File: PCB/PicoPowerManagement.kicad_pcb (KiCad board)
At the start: 2 copper layers, 101 x 71.5 mm, 21 parts, among them J1 Raspberry Pi 5 GPIO, J10 UART Header, J11 ATX 24P Connection, J12 Pi Power, J13 Barrel_Jack, J2 Raspberry Pi Pico, J3 DisplayPowerSwitch, J4 Pi1PowerSwitch, J5 Pi2PowerSwitch, J6 Pi4PowerSwitch, J7 NAS Fan 1, J8 NAS Fan 2, J9 Pi3PowerSwitch, Q1 2N3904, SW1 Power, U1 LSF0101DRYR, U2 LSF0101DRYR

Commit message: Add initial implementation of PicoPowerManagement project with API and client setup
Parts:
- removed J1: Raspberry Pi 5 GPIO, Connector_PinHeader_2.54mm:PinHeader_2x20_P2.54mm_Vertical
- J12: footprint Connector_PinHeader_2.54mm:PinHeader_2x05_P2.54mm_Vertical -> Connector_PinHeader_2.54mm:PinHeader_2x10_P2.54mm_Vertical
- moved Q1 4.09 mm to (134.0, 76.0)
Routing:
- net +5V: track 159.3 -> 148.0 mm
- net /PSU_ON: track 24.4 -> 28.0 mm
- net /PS_ON#: track 6.46 -> 8.97 mm
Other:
- board size 101 x 71.5 mm -> 78 x 70.5 mm

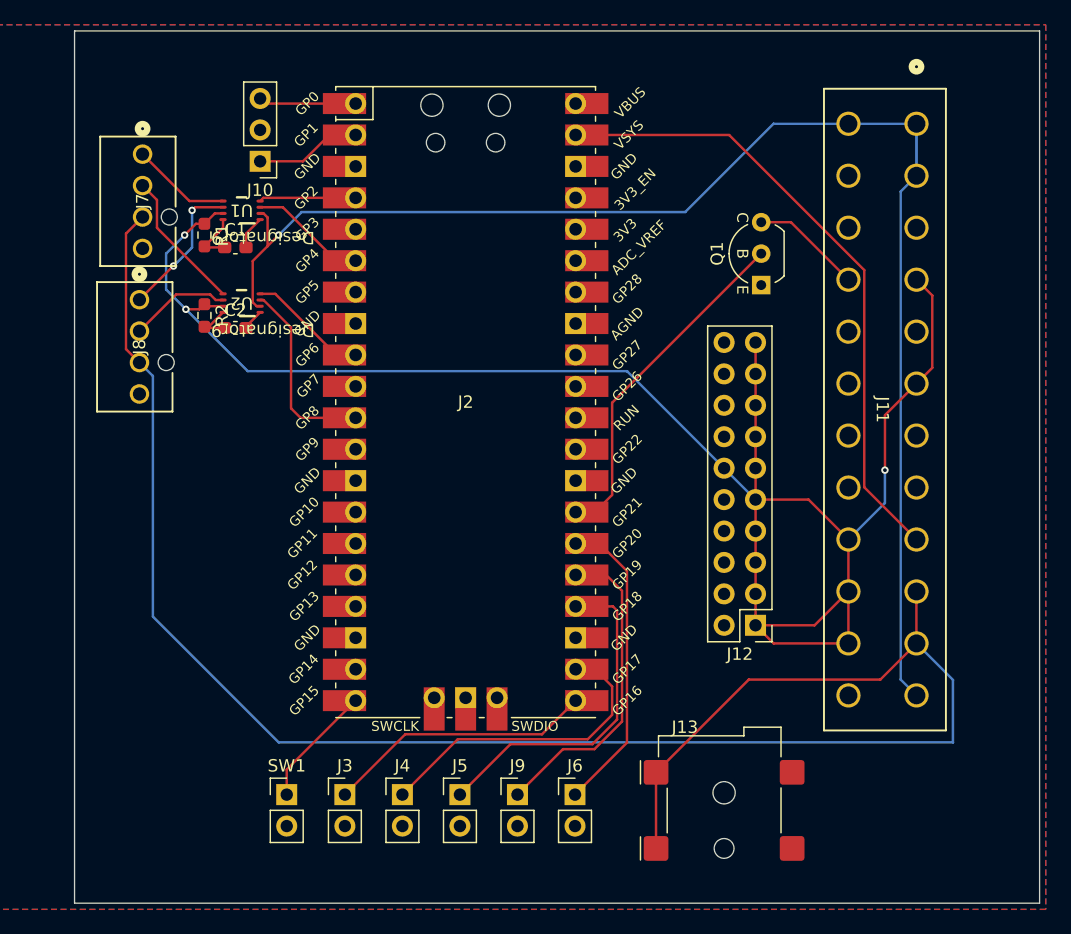
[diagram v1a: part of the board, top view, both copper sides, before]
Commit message: Add UART and pin setup functionality for PicoPowerManagement project
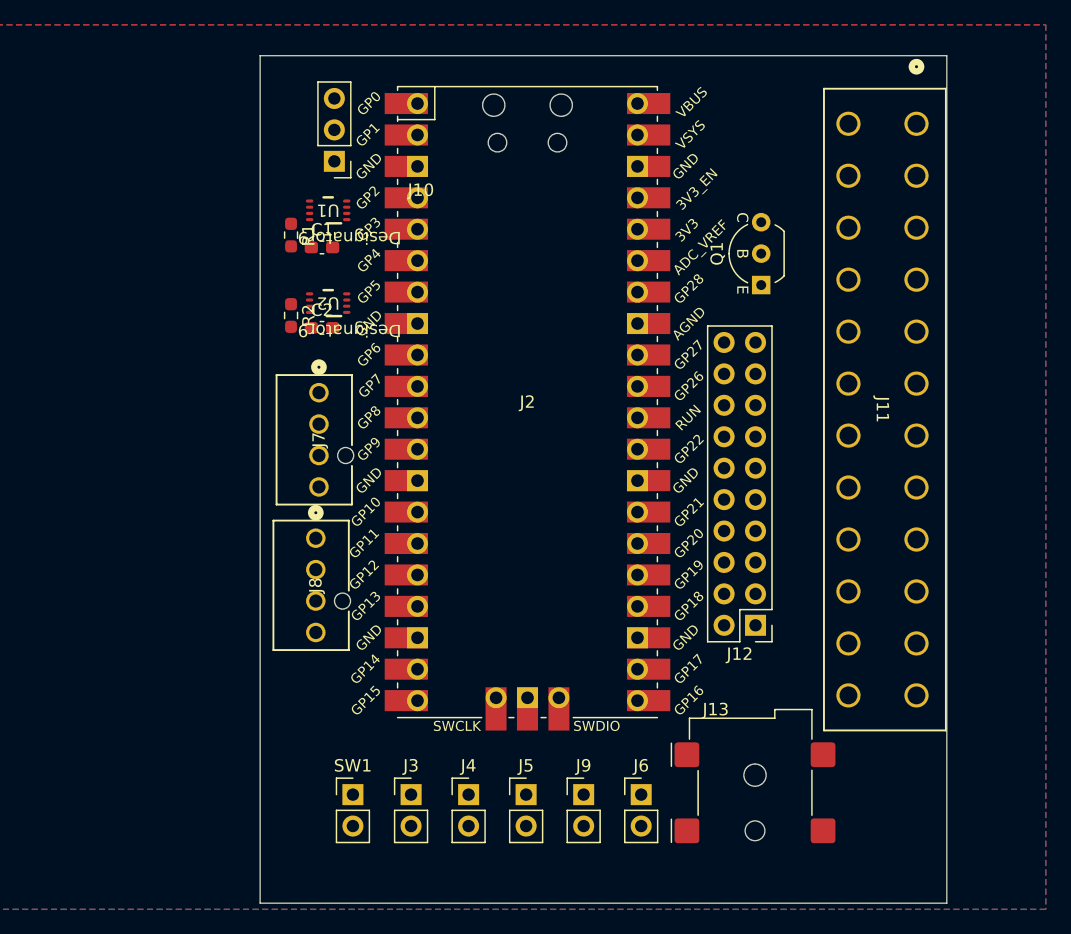
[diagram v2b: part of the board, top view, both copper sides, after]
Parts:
- moved J7 24.0 mm to (98.3, 84.7)
- moved J8 24.0 mm to (98.0, 96.5)
- moved C1 7.00 mm to (98.5, 73.0)
- moved C2 7.00 mm to (98.5, 79.5)
- moved R1 7.00 mm to (96.0, 72.0)
- moved R2 7.00 mm to (96.0, 78.5)
- moved U1 7.00 mm to (99.0, 70.0)
- moved U2 7.00 mm to (99.0, 77.5)
- moved J10 6.00 mm to (99.5, 66.0)
- moved J3 5.35 mm to (105.7, 117.2)
- moved J9 5.35 mm to (119.7, 117.2)
- moved J4 5.35 mm to (110.3, 117.2)
- moved J5 5.35 mm to (115.0, 117.2)
- moved J6 5.35 mm to (124.3, 117.2)
- moved SW1 5.35 mm to (101.0, 117.2)
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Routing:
- net +5V: track 148.0 -> 0.00 mm, vias 3 -> 0
- net +12V: track 147.6 -> 0.00 mm
- net +3.3V: track 112.6 -> 0.00 mm, vias 1 -> 0
- net /+5VDC_Standby: track 51.4 -> 0.00 mm
- net /PSU_ON: track 28.0 -> 0.00 mm
- net /Pi2_On: track 27.5 -> 0.00 mm
- net /Pi3_On: track 25.7 -> 0.00 mm
- net /Pi1_On: track 25.4 -> 0.00 mm
- net /Pi4_On: track 24.9 -> 0.00 mm
- net /Display_On: track 21.8 -> 0.00 mm
- net /3v3RPMSignal2: track 15.5 -> 0.00 mm
- net /5V PWM2: track 11.6 -> 0.00 mm, vias 2 -> 0
- net /RPM Signal1: track 11.4 -> 0.00 mm
- net Net-(J2-GPIO15): track 9.90 -> 0.00 mm
- net /3v3RPMSignal1: track 9.77 -> 0.00 mm
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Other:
- board size 78 x 70.5 mm -> 55.5 x 68.5 mm

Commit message: revamping
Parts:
- removed SW1: Power, Connector_PinHeader_2.54mm:PinHeader_1x02_P2.54mm_Vertical
- added C10: 0.1uF, Capacitor_SMD:C_0603_1608Metric_Pad1.08x0.95mm_HandSolder, F.Cu at (238.3, 32.9)
- added C11: 200pF, Capacitor_SMD:C_0603_1608Metric_Pad1.08x0.95mm_HandSolder, F.Cu at (235.3, 36.4)
- added C12: 200pF, Capacitor_SMD:C_0603_1608Metric_Pad1.08x0.95mm_HandSolder, F.Cu at (236.3, 29.4)
- added C13: 10uF, Capacitor_SMD:C_0603_1608Metric_Pad1.08x0.95mm_HandSolder, F.Cu at (208.6, 30.5)
- added C14: 0.1uF, Capacitor_SMD:C_0603_1608Metric_Pad1.08x0.95mm_HandSolder, F.Cu at (208.6, 32.0)
- added C15: 200pF, Capacitor_SMD:C_0603_1608Metric_Pad1.08x0.95mm_HandSolder, F.Cu at (205.1, 35.0)
- added C16: 200pF, Capacitor_SMD:C_0603_1608Metric_Pad1.08x0.95mm_HandSolder, F.Cu at (206.6, 28.0)
- added C17: 0.1uF, Capacitor_SMD:C_0603_1608Metric_Pad1.08x0.95mm_HandSolder, F.Cu at (202.3, 129.8)
- added C18: 10uF, Capacitor_SMD:C_0603_1608Metric_Pad1.08x0.95mm_HandSolder, F.Cu at (193.8, 128.3)
- added C19: 1uF, Capacitor_SMD:C_0603_1608Metric_Pad1.08x0.95mm_HandSolder, F.Cu at (202.3, 131.3)
- added C20: 0.1uF, Capacitor_SMD:C_0603_1608Metric_Pad1.08x0.95mm_HandSolder, F.Cu at (193.8, 126.8)
- added C21: 200pF, Capacitor_SMD:C_0603_1608Metric_Pad1.08x0.95mm_HandSolder, F.Cu at (197.8, 124.3)
- added C22: 200pF, Capacitor_SMD:C_0603_1608Metric_Pad1.08x0.95mm_HandSolder, F.Cu at (195.8, 131.3)
- added C23: 0.1uF, Capacitor_SMD:C_0603_1608Metric_Pad1.08x0.95mm_HandSolder, F.Cu at (178.3, 130.7)
- added C24: 10uF, Capacitor_SMD:C_0603_1608Metric_Pad1.08x0.95mm_HandSolder, F.Cu at (169.8, 128.7)
- added C25: 1uF, Capacitor_SMD:C_0603_1608Metric_Pad1.08x0.95mm_HandSolder, F.Cu at (178.3, 132.2)
- added C26: 0.1uF, Capacitor_SMD:C_0603_1608Metric_Pad1.08x0.95mm_HandSolder, F.Cu at (169.8, 127.2)
- added C27: 200pF, Capacitor_SMD:C_0603_1608Metric_Pad1.08x0.95mm_HandSolder, F.Cu at (173.8, 124.7)
- added C28: 200pF, Capacitor_SMD:C_0603_1608Metric_Pad1.08x0.95mm_HandSolder, F.Cu at (172.3, 131.7)
- added C29: 0.1uF, Capacitor_SMD:C_0603_1608Metric_Pad1.08x0.95mm_HandSolder, F.Cu at (140.3, 129.8)
- added C3: 0.1uF, Capacitor_SMD:C_0603_1608Metric_Pad1.08x0.95mm_HandSolder, F.Cu at (45.5, 56.5)
- added C30: 10uF, Capacitor_SMD:C_0603_1608Metric_Pad1.08x0.95mm_HandSolder, F.Cu at (148.8, 131.3)
- added C31: 1uF, Capacitor_SMD:C_0603_1608Metric_Pad1.08x0.95mm_HandSolder, F.Cu at (140.3, 128.3)
- added C32: 0.1uF, Capacitor_SMD:C_0603_1608Metric_Pad1.08x0.95mm_HandSolder, F.Cu at (148.8, 132.8)
- added C33: 200pF, Capacitor_SMD:C_0603_1608Metric_Pad1.08x0.95mm_HandSolder, F.Cu at (143.8, 125.3)
- added C34: 200pF, Capacitor_SMD:C_0603_1608Metric_Pad1.08x0.95mm_HandSolder, F.Cu at (142.8, 132.3)
- added C35: 0.1uF, Capacitor_SMD:C_0603_1608Metric_Pad1.08x0.95mm_HandSolder, F.Cu at (41.4, 53.0)
- added C36: 0.1uF, Capacitor_SMD:C_0603_1608Metric_Pad1.08x0.95mm_HandSolder, F.Cu at (207.1, 39.0)
- added C37: 0.1uF, Capacitor_SMD:C_0603_1608Metric_Pad1.08x0.95mm_HandSolder, F.Cu at (174.3, 125.7)
- added C39: 0.1uF, Capacitor_SMD:C_0603_1608Metric_Pad1.08x0.95mm_HandSolder, F.Cu at (206.1, 41.0)
- added C4: 10uF, Capacitor_SMD:C_0603_1608Metric_Pad1.08x0.95mm_HandSolder, F.Cu at (53.5, 57.7)
- added C40: 0.1uF, Capacitor_SMD:C_0603_1608Metric_Pad1.08x0.95mm_HandSolder, F.Cu at (173.8, 126.2)
- added C41: 0.1uF, Capacitor_SMD:C_0603_1608Metric_Pad1.08x0.95mm_HandSolder, F.Cu at (233.8, 33.9)
- added C42: 0.1uF, Capacitor_SMD:C_0603_1608Metric_Pad1.08x0.95mm_HandSolder, F.Cu at (197.3, 126.3)
- added C43: 0.1uF, Capacitor_SMD:C_0603_1608Metric_Pad1.08x0.95mm_HandSolder, F.Cu at (144.3, 127.3)
- added C44: 0.1uF, Capacitor_SMD:C_0603_1608Metric_Pad1.08x0.95mm_HandSolder, F.Cu at (234.3, 33.4)
- added C45: 0.1uF, Capacitor_SMD:C_0603_1608Metric_Pad1.08x0.95mm_HandSolder, F.Cu at (197.8, 126.3)
- added C46: 0.1uF, Capacitor_SMD:C_0603_1608Metric_Pad1.08x0.95mm_HandSolder, F.Cu at (141.3, 128.3)
- added C5: 1uF, Capacitor_SMD:C_0603_1608Metric_Pad1.08x0.95mm_HandSolder, F.Cu at (45.5, 55.0)
- added C6: 0.1uF, Capacitor_SMD:C_0603_1608Metric_Pad1.08x0.95mm_HandSolder, F.Cu at (53.5, 59.0)
- added C7: 200pF, Capacitor_SMD:C_0603_1608Metric_Pad1.08x0.95mm_HandSolder, F.Cu at (53.5, 60.4)
- added C8: 200pF, Capacitor_SMD:C_0603_1608Metric_Pad1.08x0.95mm_HandSolder, F.Cu at (53.5, 56.4)
- added C9: 10uF, Capacitor_SMD:C_0603_1608Metric_Pad1.08x0.95mm_HandSolder, F.Cu at (238.3, 31.4)
- added D1: D_Small, Diode_SMD:D_0603_1608Metric_Pad1.05x0.95mm_HandSolder, F.Cu at (39.9, 60.0)
- added D10: D_Small, Diode_SMD:D_0603_1608Metric_Pad1.05x0.95mm_HandSolder, F.Cu at (236.3, 32.4)
- added D11: D_Small, Diode_SMD:D_0603_1608Metric_Pad1.05x0.95mm_HandSolder, F.Cu at (199.3, 126.8)
- added D12: D_Small, Diode_SMD:D_0603_1608Metric_Pad1.05x0.95mm_HandSolder, F.Cu at (138.8, 127.8)
- added D2: D_Small, Diode_SMD:D_0603_1608Metric_Pad1.05x0.95mm_HandSolder, F.Cu at (204.1, 38.5)
- added D3: D_Small, Diode_SMD:D_0603_1608Metric_Pad1.05x0.95mm_HandSolder, F.Cu at (171.3, 124.7)
- added D4: D_Small, Diode_SMD:D_0603_1608Metric_Pad1.05x0.95mm_HandSolder, F.Cu at (36.4, 60.0)
- added D5: D_Small, Diode_SMD:D_0603_1608Metric_Pad1.05x0.95mm_HandSolder, F.Cu at (205.1, 40.0)
- added D6: D_Small, Diode_SMD:D_0603_1608Metric_Pad1.05x0.95mm_HandSolder, F.Cu at (173.8, 124.7)
- added D7: D_Small, Diode_SMD:D_0603_1608Metric_Pad1.05x0.95mm_HandSolder, F.Cu at (233.3, 33.9)
- added D8: D_Small, Diode_SMD:D_0603_1608Metric_Pad1.05x0.95mm_HandSolder, F.Cu at (199.3, 127.3)
- added D9: D_Small, Diode_SMD:D_0603_1608Metric_Pad1.05x0.95mm_HandSolder, F.Cu at (142.8, 128.3)
- added J1: UART Header, Connector_PinHeader_2.54mm:PinHeader_1x03_P2.54mm_Vertical, F.Cu at (173.5, 61.5)
- added Q10: PMOS, SI2312:SOT23, F.Cu at (144.8, 129.3)
- added Q11: PMOS, SI2312:SOT23, F.Cu at (234.3, 32.9)
- added Q12: PMOS, SI2312:SOT23, F.Cu at (198.3, 127.3)
- added Q13: PMOS, SI2312:SOT23, F.Cu at (141.8, 128.8)
- added Q2: PMOS, SI2312:SOT23, F.Cu at (39.9, 62.5)
- added Q3: PMOS, SI2312:SOT23, F.Cu at (204.1, 41.0)
- added Q4: PMOS, SI2312:SOT23, F.Cu at (172.8, 126.2)
- added Q5: PMOS, SI2312:SOT23, F.Cu at (36.4, 62.5)
- added Q6: PMOS, SI2312:SOT23, F.Cu at (206.6, 40.0)
- added Q7: PMOS, SI2312:SOT23, F.Cu at (172.3, 126.7)
- added Q8: PMOS, SI2312:SOT23, F.Cu at (233.8, 32.9)
- added Q9: PMOS, SI2312:SOT23, F.Cu at (199.8, 126.8)
- added R10: 0.25, Resistor_SMD:R_0603_1608Metric_Pad0.98x0.95mm_HandSolder, F.Cu at (204.1, 44.0)
- added R11: 0.25, Resistor_SMD:R_0603_1608Metric_Pad0.98x0.95mm_HandSolder, F.Cu at (173.3, 125.2)
- added R13: 0.25, Resistor_SMD:R_0603_1608Metric_Pad0.98x0.95mm_HandSolder, F.Cu at (202.6, 40.0)
- added R14: 0.25, Resistor_SMD:R_0603_1608Metric_Pad0.98x0.95mm_HandSolder, F.Cu at (173.3, 124.7)
- added R15: 0.25, Resistor_SMD:R_0603_1608Metric_Pad0.98x0.95mm_HandSolder, F.Cu at (234.8, 34.4)
- added R16: 0.25, Resistor_SMD:R_0603_1608Metric_Pad0.98x0.95mm_HandSolder, F.Cu at (199.3, 126.8)
- added R17: 0.25, Resistor_SMD:R_0603_1608Metric_Pad0.98x0.95mm_HandSolder, F.Cu at (144.3, 129.3)
- added R18: 0.25, Resistor_SMD:R_0603_1608Metric_Pad0.98x0.95mm_HandSolder, F.Cu at (229.8, 33.4)
- added R19: 0.25, Resistor_SMD:R_0603_1608Metric_Pad0.98x0.95mm_HandSolder, F.Cu at (199.3, 125.3)
- added R20: 0.25, Resistor_SMD:R_0603_1608Metric_Pad0.98x0.95mm_HandSolder, F.Cu at (141.3, 128.3)
- added R3: 4.7k, Resistor_SMD:R_0603_1608Metric_Pad0.98x0.95mm_HandSolder, F.Cu at (45.5, 58.0)
- added R4: 4.7k, Resistor_SMD:R_0603_1608Metric_Pad0.98x0.95mm_HandSolder, F.Cu at (229.8, 32.4)
- added R5: 4.7k, Resistor_SMD:R_0603_1608Metric_Pad0.98x0.95mm_HandSolder, F.Cu at (200.6, 30.5)
- added R6: 4.7k, Resistor_SMD:R_0603_1608Metric_Pad0.98x0.95mm_HandSolder, F.Cu at (202.3, 128.3)
- added R7: 4.7k, Resistor_SMD:R_0603_1608Metric_Pad0.98x0.95mm_HandSolder, F.Cu at (178.3, 129.2)
- added R8: 4.7k, Resistor_SMD:R_0603_1608Metric_Pad0.98x0.95mm_HandSolder, F.Cu at (148.8, 129.8)
- added R9: 0.25, Resistor_SMD:R_0603_1608Metric_Pad0.98x0.95mm_HandSolder, F.Cu at (36.4, 53.0)
- added U10: FUSB302B10MPX, FUSB302:MLP14_2P5X2P5_ONS, F.Cu at (174.2, 128.7)
- added U11: FUSB302B11MPX, FUSB302:MLP14_2P5X2P5_ONS, F.Cu at (144.8, 129.3)
- added U12: LM338T/NOPB, LM338:T03B_TEX, F.Cu at (35.4, 57.0)
- added U13: LM338T/NOPB, LM338:T03B_TEX, F.Cu at (201.9, 41.5)
- added U14: LM338T/NOPB, LM338:T03B_TEX, F.Cu at (175.4, 124.2)
- added U16: LM338T/NOPB, LM338:T03B_TEX, F.Cu at (203.9, 42.8)
- added U17: LM338T/NOPB, LM338:T03B_TEX, F.Cu at (175.9, 125.2)
- added U18, U21: LM338T/NOPB, LM338:T03B_TEX, F.Cu at (232.2, 34.4)
- added U19: LM338T/NOPB, LM338:T03B_TEX, F.Cu at (201.4, 126.3)
- added U20: LM338T/NOPB, LM338:T03B_TEX, F.Cu at (146.4, 128.3)
- added U22: LM338T/NOPB, LM338:T03B_TEX, F.Cu at (200.9, 126.3)
- added U23: LM338T/NOPB, LM338:T03B_TEX, F.Cu at (143.9, 127.8)
- added U3: LP5810ADSDR, LP5810:DSD0008B-MFG, F.Cu at (172.5, 104.0)
- added U4: LSF0101DRYR, LSF0102DCUR:DCU0008A_L, F.Cu at (159.5, 73.0)
- added U5: LSF0101DRYR, LSF0102DCUR:DCU0008A_L, F.Cu at (159.5, 77.5)
- added U6: FUSB002B01MPX, FUSB302:MLP14_2P5X2P5_ONS, F.Cu at (49.5, 58.5)
- added U7: FUSB002B10MPX, FUSB302:MLP14_2P5X2P5_ONS, F.Cu at (234.2, 32.4)
- added U8: FUSB002B11MPX, FUSB302:MLP14_2P5X2P5_ONS, F.Cu at (204.4, 31.0)
- added U9: FUSB302B01MPX, FUSB302:MLP14_2P5X2P5_ONS, F.Cu at (198.1, 128.3)
- J10: value UART Header -> GSB3CA11310DSHR; footprint Connector_PinHeader_2.54mm:PinHeader_1x03_P2.54mm_Vertical -> GSB3CA11310DSHR:AMPHENOL_GSB3CA11310DSHR
- J11: value ATX 24P Connection -> GSB3CA11310DSHR; footprint Mini-fit Jr:CONN_5566-24_MOL -> GSB3CA11310DSHR:AMPHENOL_GSB3CA11310DSHR
- J12: value Pi Power -> GSB3CA11310DSHR; footprint Connector_PinHeader_2.54mm:PinHeader_2x10_P2.54mm_Vertical -> GSB3CA11310DSHR:AMPHENOL_GSB3CA11310DSHR
- J13: value Barrel_Jack -> GSB3CA11310DSHR; footprint Connector_BarrelJack:BarrelJack_Wuerth_694108106102_2.5x5.5mm -> GSB3CA11310DSHR:AMPHENOL_GSB3CA11310DSHR
- J2: value Raspberry Pi Pico -> DEBUG; footprint MCU_RaspberryPi_and_Boards:RPi_Pico_SMD_TH -> Connector_PinHeader_2.54mm:PinHeader_1x03_P2.54mm_Vertical
- J3: value DisplayPowerSwitch -> SwitchLEDS; footprint Connector_PinHeader_2.54mm:PinHeader_1x02_P2.54mm_Vertical -> Connector_PinHeader_2.54mm:PinHeader_2x04_P2.54mm_Vertical
- J4: value Pi1PowerSwitch -> PowerSwitch; footprint Connector_PinHeader_2.54mm:PinHeader_1x02_P2.54mm_Vertical -> Connector_PinHeader_2.54mm:PinHeader_2x06_P2.54mm_Vertical
- J5: value Pi2PowerSwitch -> NAS Fan 1; footprint Connector_PinHeader_2.54mm:PinHeader_1x02_P2.54mm_Vertical -> Fan Connector:CONN_SD-47053-001_H10p00_MOL
- J6: value Pi4PowerSwitch -> NAS Fan 2; footprint Connector_PinHeader_2.54mm:PinHeader_1x02_P2.54mm_Vertical -> Fan Connector:CONN_SD-47053-001_H10p00_MOL
- J7: value NAS Fan 1 -> ATX 24P Connection; footprint Fan Connector:CONN_SD-47053-001_H10p00_MOL -> Mini-fit Jr:CONN_5566-24_MOL
- J8: value NAS Fan 2 -> GSB3CA11310DSHR; footprint Fan Connector:CONN_SD-47053-001_H10p00_MOL -> GSB3CA11310DSHR:AMPHENOL_GSB3CA11310DSHR
- J9: value Pi3PowerSwitch -> GSB3CA11310DSHR; footprint Connector_PinHeader_2.54mm:PinHeader_1x02_P2.54mm_Vertical -> GSB3CA11310DSHR:AMPHENOL_GSB3CA11310DSHR
- Q1: footprint PCM_Package_TO_SOT_THT_AKL:TO-92_Inline_Wide_EBC -> Package_TO_SOT_THT:TO-92-2_Wide
- U1: value LSF0101DRYR -> ~; footprint LSF0102DCUR:DCU0008A_L -> MCU_RaspberryPi_and_Boards:PGA2350
- U2: value LSF0101DRYR -> LP5810ADSDR; footprint LSF0102DCUR:DCU0008A_L -> LP5810:DSD0008B-MFG
- moved J9 147.8 mm to (234.5, 24.2), turned to 180 degrees
- moved J7 139.3 mm to (237.5, 87.4), turned to 0 degrees
- moved J10 113.8 mm to (204.8, 22.9)
- moved J11 89.6 mm to (198.0, 136.3), turned to 0 degrees
- moved U2 77.0 mm to (172.5, 100.5), turned to 0 degrees
- moved J8 74.3 mm to (40.2, 49.9), turned to 180 degrees
- moved J2 66.9 mm to (177.5, 61.5)
- moved J3 66.1 mm to (171.2, 108.7)
- moved U1 62.9 mm to (36.1, 69.1), turned to 0 degrees
- moved R1 60.6 mm to (156.5, 74.5)
- moved C1 60.5 mm to (159.0, 75.0)
- moved R2 60.5 mm to (156.5, 79.0)
- moved C2 60.5 mm to (159.0, 79.5)
- moved J4 57.7 mm to (157.2, 83.7)
- moved Q1 56.8 mm to (189.5, 63.9), turned to 0 degrees
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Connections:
- C1 pad 1: Net-(U1-EN) -> Net-(U4-EN)
- C2 pad 1: Net-(U2-EN) -> Net-(U5-EN)
- J2 pad 1: /UART TX -> /SWDIO
- J2 pad 2: /UART RX -> GND
- J2 pad 3: GND -> /SWCLK
- J3 pad 1: /Display_On -> /PWR_R
- J3 pad 2: GND -> /RESET_R
- J4 pad 1: /Pi1_On -> /Display_On
- J5 pad 1: /Pi2_On -> /5V PWM1
- J5 pad 2: GND -> /RPM Signal1
- J6 pad 1: /Pi4_On -> /5V PWM2
- J6 pad 2: GND -> /RPM Signal2
- J7 pad 1: /5V PWM1 -> +3.3V
- J7 pad 2: /RPM Signal1 -> +3.3V
- J7 pad 3: +12V -> GND
- J7 pad 4: GND -> +5V
- R1 pad 2: Net-(U1-EN) -> Net-(U4-EN)
- R2 pad 2: Net-(U2-EN) -> Net-(U5-EN)
- U1 pad 1: GND -> /UART RX
- U1 pad 2: +3.3V -> /3v3PWM1
- U1 pad 3: /3v3PWM2 -> /3v3RPMSignal1
- U1 pad 4: /3v3PWM1 -> /3v3PWM2
- U1 pad 5: /5V PWM1 -> /3v3RPMSignal2
- U1 pad 6: /5V PWM2 -> /Display_On
- U1 pad 7: +5V -> /Pi1_On
- U1 pad 8: Net-(U1-EN) -> /Pi2_On
- U2 pad 1: GND -> +3.3V
- U2 pad 2: +3.3V -> GND
- U2 pad 3: /3v3RPMSignal2 -> SCL0
- U2 pad 4: /3v3RPMSignal1 -> SDA0
- U2 pad 5: /RPM Signal1 -> unconnected-(U2-OUT3-Pad5)
- U2 pad 6: /RPM Signal2 -> /PWR_B
- U2 pad 7: +5V -> /PWR_G
- U2 pad 8: Net-(U2-EN) -> /PWR_R
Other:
- board size 55.5 x 68.5 mm -> 85 x 56 mm

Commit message: confused now
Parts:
- removed C45, C46: 0.1uF, Capacitor_SMD:C_0603_1608Metric_Pad1.08x0.95mm_HandSolder
- removed R13, R14, R18, R19, R20: 0.25, Resistor_SMD:R_0603_1608Metric_Pad0.98x0.95mm_HandSolder
- removed U16, U17, U21, U22, U23: LM338T/NOPB, LM338:T03B_TEX
- added C38: 0.1uF, Capacitor_SMD:C_0603_1608Metric_Pad1.08x0.95mm_HandSolder, F.Cu at (69.8, 52.3)
- C39, C44: value 0.1uF -> 1uF
- moved J9 166.4 mm to (68.4, 32.6)
- moved R15 164.5 mm to (70.4, 36.6)
- moved U18 162.8 mm to (69.5, 40.6)
- moved U7 161.8 mm to (73.9, 54.4)
- moved R4 161.4 mm to (69.8, 53.8)
- moved C10 161.3 mm to (78.5, 54.9)
- moved C9 161.3 mm to (78.5, 53.3)
- moved C12 159.4 mm to (78.5, 51.8)
- moved Q8 158.4 mm to (76.1, 48.0), turned to 180 degrees
- moved C11 158.1 mm to (78.5, 56.4), turned to 0 degrees
- moved C41 157.9 mm to (75.9, 36.6)
- moved D7 157.6 mm to (76.1, 45.0)
- moved D10 156.4 mm to (80.4, 45.0)
- moved C44 154.7 mm to (83.1, 66.0)
- moved Q11 154.7 mm to (80.3, 48.0), turned to 180 degrees
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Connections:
- C36 pad 1: +5V -> Net-(D2-K)
- C37 pad 1: +5V -> Net-(D3-K)
- C39 pad 1: +12V -> +3.3V
- C40 pad 1: +12V -> +3.3V
- C41 pad 1: +5V -> Net-(D10-K)
- C42 pad 1: +5V -> Net-(D11-K)
- C43 pad 1: +5V -> Net-(D12-K)
- C44 pad 1: +12V -> +3.3V
- D10 pad 1: /USB1_VBUS -> Net-(D10-K)
- D11 pad 1: /USB3_VBUS -> Net-(D11-K)
- D12 pad 1: /USB5_VBUS -> Net-(D12-K)
- D2 pad 1: /USB2_VBUS -> Net-(D2-K)
- D3 pad 1: /USB4_VBUS -> Net-(D3-K)
- D5 pad 1: /USB2_VBUS -> Net-(D2-K)
- D6 pad 1: /USB4_VBUS -> Net-(D3-K)
- D7 pad 1: /USB1_VBUS -> Net-(D10-K)
- D8 pad 1: /USB3_VBUS -> Net-(D11-K)
- D9 pad 1: /USB5_VBUS -> Net-(D12-K)
- Q10 pad 3: Net-(Q10-S) -> +5V
- Q11 pad 3: Net-(Q11-S) -> +12V
- Q12 pad 3: Net-(Q12-S) -> +12V
- Q13 pad 3: Net-(Q13-S) -> +12V
- Q3 pad 3: Net-(Q3-S) -> +5V
- Q4 pad 3: Net-(Q4-S) -> +5V
- Q6 pad 3: Net-(Q6-S) -> +12V
- Q7 pad 3: Net-(Q7-S) -> +12V
- Q8 pad 3: Net-(Q8-S) -> +5V
- Q9 pad 3: Net-(Q9-S) -> +5V
- R10 pad 2: Net-(Q3-S) -> /USB2_VBUS
- R11 pad 2: Net-(Q4-S) -> /USB4_VBUS
- R15 pad 2: Net-(Q8-S) -> /USB1_VBUS
- R16 pad 2: Net-(Q9-S) -> /USB3_VBUS
- R17 pad 2: Net-(Q10-S) -> /USB5_VBUS
- U13 pad 2: Net-(Q3-S) -> /USB2_VBUS
- U13 pad 3: +5V -> Net-(D2-K)
- U14 pad 2: Net-(Q4-S) -> /USB4_VBUS
- U14 pad 3: +5V -> Net-(D3-K)
- U18 pad 2: Net-(Q8-S) -> /USB1_VBUS
- U18 pad 3: +5V -> Net-(D10-K)
- U19 pad 2: Net-(Q9-S) -> /USB3_VBUS
- U19 pad 3: +5V -> Net-(D11-K)
- U20 pad 2: Net-(Q10-S) -> /USB5_VBUS
- U20 pad 3: +5V -> Net-(D12-K)
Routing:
- net /USB0/USB1_CC2: track 0.00 -> 35.1 mm
- net Net-(D12-K): track 0.00 -> 33.1 mm
- net /USB0/USB0_CC2: track 0.00 -> 32.5 mm
- net +3.3V: track 0.00 -> 29.8 mm
- net /USB0/USB0_CC1: track 0.00 -> 29.0 mm
- net Net-(D3-K): track 0.00 -> 27.2 mm
- net /USB1_VBUS: track 0.00 -> 24.0 mm
- net /USB0_VBUS: track 0.00 -> 23.6 mm
- net Net-(D1-K): track 0.00 -> 22.0 mm
- net /USB5_VBUS: track 0.00 -> 20.3 mm
- net Net-(D11-K): track 0.00 -> 20.2 mm
- net /USB4_VBUS: track 0.00 -> 16.6 mm
- net Net-(D10-K): track 0.00 -> 15.5 mm
- net Net-(D2-K): track 0.00 -> 14.5 mm
- net /USB3_VBUS: track 0.00 -> 12.2 mm
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- added copper zone on In1.Cu, net GND
- added copper zone on In2.Cu, net GND
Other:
- board size 85 x 56 mm -> 138.7 x 119.1 mm
- copper layers 2 -> 4
